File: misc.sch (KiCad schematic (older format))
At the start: 12 parts, among them J11 USB_OTG, U3 RT9193-28, U4 XC6206P302MR

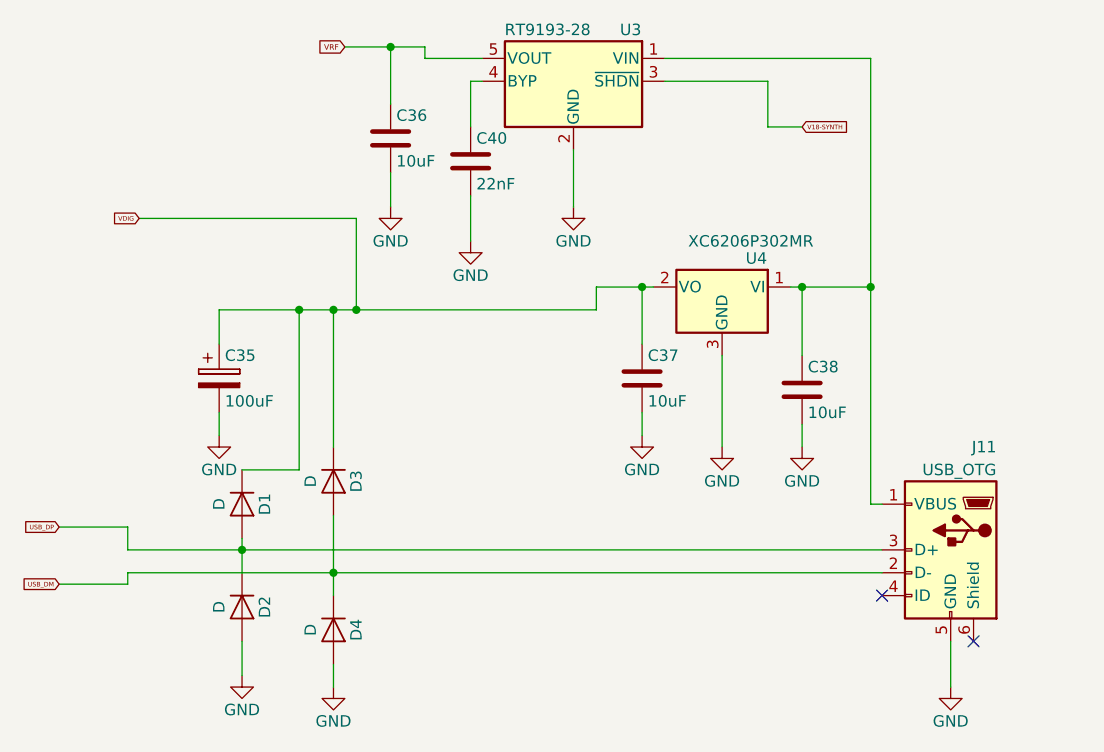
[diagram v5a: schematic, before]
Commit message: use bav99 replace diode
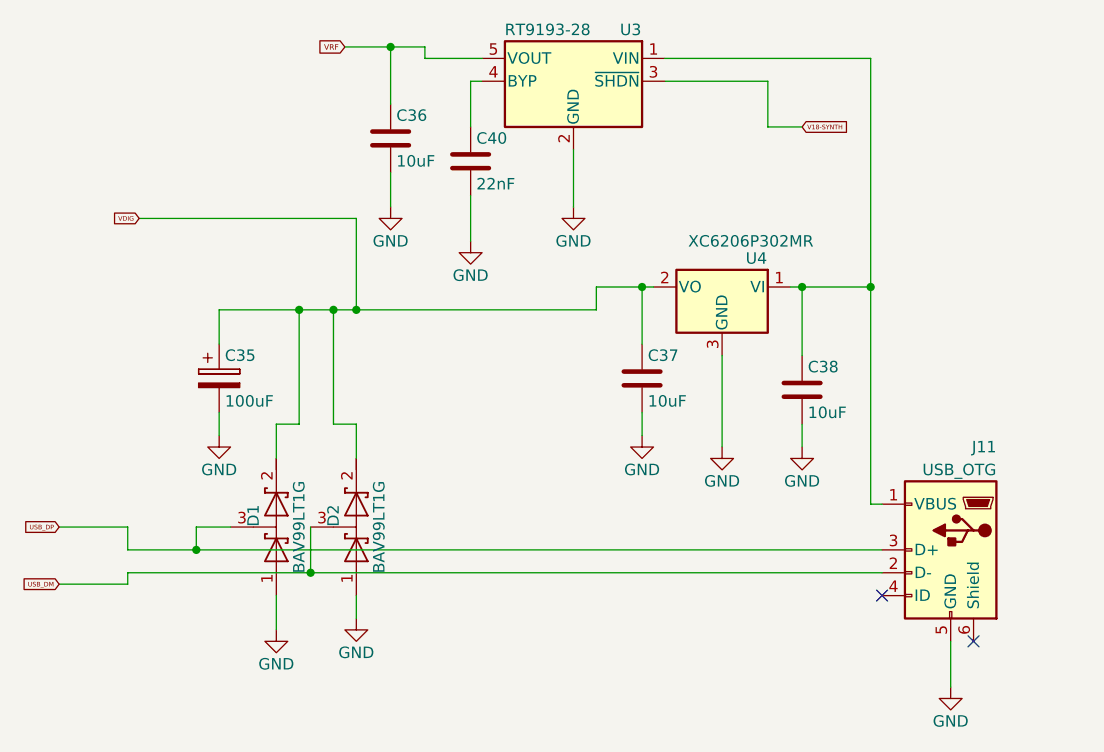
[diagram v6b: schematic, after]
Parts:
- removed D1, D2, D3, D4: D, Diodes_SMD:D_0805, symbol D
- added D1, D2: BAV99LT1G, TO_SOT_Packages_SMD:SOT-23, symbol D_Schottky_x2_Serial_AKC
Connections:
- net GND: now also D1.1 (A), D2.1 (A)
- net USB_DM: now also D2.3 (common)
- net USB_DP: now also D1.3 (common)
- net VDIG: now also D1.2 (K), D2.2 (K)
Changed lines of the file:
@@
 $EndDescr
 $Comp
-L D D1
-U 1 1 5C690C27
-P 4700 3500
-F 0 "D1" H 4700 3600 50  0000 C CNN
-F 1 "D" H 4700 3400 50  0000 C CNN
-F 2 "Diodes_SMD:D_0805" H 4700 3500 50  0001 C CNN
-F 3 "" H 4700 3500 50  0001 C CNN
-	1    4700 3500
-	0    1    1    0
-$EndComp
-$Comp
-L D D2
-U 1 1 5C690CDD
-P 4700 3950
-F 0 "D2" H 4700 4050 50  0000 C CNN
-F 1 "D" H 4700 3850 50  0000 C CNN
-F 2 "Diodes_SMD:D_0805" H 4700 3950 50  0001 C CNN
-F 3 "" H 4700 3950 50  0001 C CNN
-	1    4700 3950
-	0    1    1    0
-$EndComp
-$Comp
-L D D4
-U 1 1 5C690D30
-P 5100 4050
-F 0 "D4" H 5100 4150 50  0000 C CNN
-F 1 "D" H 5100 3950 50  0000 C CNN
-F 2 "Diodes_SMD:D_0805" H 5100 4050 50  0001 C CNN
-F 3 "" H 5100 4050 50  0001 C CNN
-	1    5100 4050
-	0    1    1    0
-$EndComp
-$Comp
-L D D3
-U 1 1 5C690DBF
-P 5100 3400
-F 0 "D3" H 5100 3500 50  0000 C CNN
-F 1 "D" H 5100 3300 50  0000 C CNN
-F 2 "Diodes_SMD:D_0805" H 5100 3400 50  0001 C CNN
-F 3 "" H 5100 3400 50  0001 C CNN
-	1    5100 3400
-	0    1    1    0
-$EndComp
-Wire Wire Line
-	4600 2650 6250 2650
-Wire Wire Line
-	5100 3250 5100 2650
-Connection ~ 5100 2650
-Wire Wire Line
-	5100 3550 5100 3900
-Wire Wire Line
-	4700 3650 4700 3800
-Wire Wire Line
-	4200 3700 7500 3700
-Connection ~ 4700 3700
-Wire Wire Line
-	4200 3800 7500 3800
-Connection ~ 5100 3800
-$Comp
-L GND #PWR037
+L GND #PWR38
 U 1 1 5C690F71
-P 4700 4250
-F 0 "#PWR037" H 4700 4000 50  0001 C CNN
-F 1 "GND" H 4700 4100 50  0000 C CNN
-F 2 "" H 4700 4250 50  0001 C CNN
-F 3 "" H 4700 4250 50  0001 C CNN
-	1    4700 4250
-	1    0    0    -1
-$EndComp
-$Comp
-L GND #PWR038
+P 4850 4050
+F 0 "#PWR38" H 4850 3800 50  0001 C CNN
+F 1 "GND" H 4850 3900 50  0000 C CNN
+F 2 "" H 4850 4050 50  0001 C CNN
+F 3 "" H 4850 4050 50  0001 C CNN
+	1    4850 4050
+	1    0    0    -1
+$EndComp
+$Comp
+L GND #PWR39
 U 1 1 5C690F9B
-P 5100 4300
-F 0 "#PWR038" H 5100 4050 50  0001 C CNN
-F 1 "GND" H 5100 4150 50  0000 C CNN
-F 2 "" H 5100 4300 50  0001 C CNN
-F 3 "" H 5100 4300 50  0001 C CNN
-	1    5100 4300
-	1    0    0    -1
-$EndComp
-Wire Wire Line
-	5100 4300 5100 4200
-Wire Wire Line
-	4700 4250 4700 4100
-Wire Wire Line
-	4700 3350 4950 3350
-Wire Wire Line
-	4950 3350 4950 2650
+P 5200 4000
+F 0 "#PWR39" H 5200 3750 50  0001 C CNN
+F 1 "GND" H 5200 3850 50  0000 C CNN
+F 2 "" H 5200 4000 50  0001 C CNN
+F 3 "" H 5200 4000 50  0001 C CNN
+	1    5200 4000
+	1    0    0    -1
+$EndComp
 Text GLabel 4250 2250 0    20   Input ~ 0
 VDIG
-Wire Wire Line
-	4250 2250 5200 2250
-Wire Wire Line
-	5200 2250 5200 2650
-Connection ~ 5200 2650
 Text GLabel 3900 3850 0    20   Input ~ 0
 USB_DM
 Text GLabel 3900 3600 0    20   Input ~ 0
 USB_DP
-Wire Wire Line
-	4200 3700 4200 3600
-Wire Wire Line
-	4200 3600 3900 3600
-Wire Wire Line
-	4200 3800 4200 3850
-Wire Wire Line
-	4200 3850 3900 3850
-$Comp
-L GND #PWR039
+$Comp
+L GND #PWR37
 U 1 1 5C6911FA
 P 4600 3200
-F 0 "#PWR039" H 4600 2950 50  0001 C CNN
+F 0 "#PWR37" H 4600 2950 50  0001 C CNN
 F 1 "GND" H 4600 3050 50  0000 C CNN
 F 2 "" H 4600 3200 50  0001 C CNN
@@
 	1    0    0    -1
 $EndComp
-Wire Wire Line
-	6450 2800 6450 2550
-Wire Wire Line
-	6250 2550 6500 2550
-Wire Wire Line
-	7100 2550 7450 2550
-Wire Wire Line
-	7150 2550 7150 2850
-$Comp
-L GND #PWR040
+$Comp
+L GND #PWR44
 U 1 1 5C691B40
 P 6800 3250
-F 0 "#PWR040" H 6800 3000 50  0001 C CNN
+F 0 "#PWR44" H 6800 3000 50  0001 C CNN
 F 1 "GND" H 6800 3100 50  0000 C CNN
 F 2 "" H 6800 3250 50  0001 C CNN
@@
 	1    0    0    -1
 $EndComp
-Wire Wire Line
-	6800 3250 6800 2850
-Wire Wire Line
-	6250 2650 6250 2550
-Connection ~ 6450 2550
-Wire Wire Line
-	7450 1550 7450 3500
-Connection ~ 7150 2550
-$Comp
-L GND #PWR041
+$Comp
+L GND #PWR43
 U 1 1 5C692086
 P 6450 3200
-F 0 "#PWR041" H 6450 2950 50  0001 C CNN
+F 0 "#PWR43" H 6450 2950 50  0001 C CNN
 F 1 "GND" H 6450 3050 50  0000 C CNN
 F 2 "" H 6450 3200 50  0001 C CNN
@@
 $EndComp
 $Comp
-L GND #PWR042
+L GND #PWR45
 U 1 1 5C6920B8
 P 7150 3250
-F 0 "#PWR042" H 7150 3000 50  0001 C CNN
+F 0 "#PWR45" H 7150 3000 50  0001 C CNN
 F 1 "GND" H 7150 3100 50  0000 C CNN
 F 2 "" H 7150 3250 50  0001 C CNN
@@
 	1    0    0    -1
 $EndComp
-Wire Wire Line
-	6450 3200 6450 3100
-Wire Wire Line
-	7150 3250 7150 3150
-$Comp
-L GND #PWR043
+$Comp
+L GND #PWR42
 U 1 1 5C69221A
 P 6150 2200
-F 0 "#PWR043" H 6150 1950 50  0001 C CNN
+F 0 "#PWR42" H 6150 1950 50  0001 C CNN
 F 1 "GND" H 6150 2050 50  0000 C CNN
 F 2 "" H 6150 2200 50  0001 C CNN
@@
 Text GLabel 5150 1500 0    24   Input ~ 0
 VRF
-Wire Wire Line
-	5500 1550 5750 1550
-Wire Wire Line
-	5500 1550 5500 1500
-Wire Wire Line
-	5500 1500 5150 1500
 Text GLabel 7150 1850 2    20   Input ~ 0
 V18-SYNTH
-Wire Wire Line
-	7150 1850 7000 1850
-Wire Wire Line
-	7000 1850 7000 1650
-Wire Wire Line
-	7000 1650 6550 1650
 $Comp
 L C C36
@@
 	1    0    0    -1
 $EndComp
-Wire Wire Line
-	5350 1750 5350 1500
-Connection ~ 5350 1500
-$Comp
-L GND #PWR044
+$Comp
+L GND #PWR40
 U 1 1 5C692712
 P 5350 2200
-F 0 "#PWR044" H 5350 1950 50  0001 C CNN
+F 0 "#PWR40" H 5350 1950 50  0001 C CNN
 F 1 "GND" H 5350 2050 50  0000 C CNN
 F 2 "" H 5350 2200 50  0001 C CNN
@@
 	1    0    0    -1
 $EndComp
-Wire Wire Line
-	5350 2200 5350 2050
-Wire Wire Line
-	6550 1550 7450 1550
-Connection ~ 7450 2550
-Wire Wire Line
-	6150 1950 6150 2200
-$Comp
-L GND #PWR045
+$Comp
+L GND #PWR46
 U 1 1 5C693D92
 P 7800 4300
-F 0 "#PWR045" H 7800 4050 50  0001 C CNN
+F 0 "#PWR46" H 7800 4050 50  0001 C CNN
 F 1 "GND" H 7800 4150 50  0000 C CNN
 F 2 "" H 7800 4300 50  0001 C CNN
@@
 	1    0    0    -1
 $EndComp
-Wire Wire Line
-	7800 4300 7800 4100
 $Comp
 L USB_OTG J11
@@
 NoConn ~ 7500 3900
 NoConn ~ 7900 4100
-Wire Wire Line
-	7450 3500 7500 3500
-Wire Wire Line
-	4600 2650 4600 2800
-Connection ~ 4950 2650
 $Comp
 L CP C35
@@
 	1    0    0    -1
 $EndComp
-Wire Wire Line
-	4600 3200 4600 3100
 $Comp
 L APE8865NR-30-HF-3 U4
@@
 $EndComp
 $Comp
-L GND #PWR046
+L GND #PWR41
 U 1 1 5CB1E8F3
 P 5700 2350
-F 0 "#PWR046" H 5700 2100 50  0001 C CNN
+F 0 "#PWR41" H 5700 2100 50  0001 C CNN
 F 1 "GND" H 5700 2200 50  0000 C CNN
 F 2 "" H 5700 2350 50  0001 C CNN
@@
 	1    0    0    -1
 $EndComp
+$Comp
+L D_Schottky_x2_Serial_AKC D1
+U 1 1 5CBC63C6
+P 4850 3600
+F 0 "D1" H 4900 3500 50  0000 C CNN
+F 1 "BAV99LT1G" H 4850 3700 50  0000 C CNN
+F 2 "TO_SOT_Packages_SMD:SOT-23" H 4850 3600 50  0001 C CNN
+F 3 "" H 4850 3600 50  0001 C CNN
+	1    4850 3600
+	0    1    -1   0
+$EndComp
+$Comp
+L D_Schottky_x2_Serial_AKC D2
+U 1 1 5CBC651E
+P 5200 3600
+F 0 "D2" H 5250 3500 50  0000 C CNN
+F 1 "BAV99LT1G" H 5200 3700 50  0000 C CNN
+F 2 "TO_SOT_Packages_SMD:SOT-23" H 5200 3600 50  0001 C CNN
+F 3 "" H 5200 3600 50  0001 C CNN
+	1    5200 3600
+	0    1    -1   0
+$EndComp
+Wire Wire Line
+	4600 2650 6250 2650
+Connection ~ 5100 2650
+Wire Wire Line
+	4200 3700 7500 3700
+Wire Wire Line
+	4200 3800 7500 3800
+Wire Wire Line
+	5200 4000 5200 3900
+Wire Wire Line
+	4850 4050 4850 3900
+Wire Wire Line
+	4250 2250 5200 2250
+Wire Wire Line
+	5200 2250 5200 2650
+Connection ~ 5200 2650
+Wire Wire Line
+	4200 3700 4200 3600
+Wire Wire Line
+	4200 3600 3900 3600
+Wire Wire Line
+	4200 3800 4200 3850
+Wire Wire Line
+	4200 3850 3900 3850
+Wire Wire Line
+	6450 2800 6450 2550
+Wire Wire Line
+	6250 2550 6500 2550
+Wire Wire Line
+	7100 2550 7450 2550
+Wire Wire Line
+	7150 2550 7150 2850
+Wire Wire Line
+	6800 3250 6800 2850
+Wire Wire Line
+	6250 2650 6250 2550
+Connection ~ 6450 2550
+Wire Wire Line
+	7450 1550 7450 3500
+Connection ~ 7150 2550
+Wire Wire Line
+	6450 3200 6450 3100
+Wire Wire Line
+	7150 3250 7150 3150
+Wire Wire Line
+	5500 1550 5750 1550
+Wire Wire Line
+	5500 1550 5500 1500
+Wire Wire Line
+	5500 1500 5150 1500
+Wire Wire Line
+	7150 1850 7000 1850
+Wire Wire Line
+	7000 1850 7000 1650
+Wire Wire Line
+	7000 1650 6550 1650
+Wire Wire Line
+	5350 1750 5350 1500
+Connection ~ 5350 1500
+Wire Wire Line
+	5350 2200 5350 2050
+Wire Wire Line
+	6550 1550 7450 1550
+Connection ~ 7450 2550
+Wire Wire Line
+	6150 1950 6150 2200
+Wire Wire Line
+	7800 4300 7800 4100
+Wire Wire Line
+	7450 3500 7500 3500
+Wire Wire Line
+	4600 2650 4600 2800
+Connection ~ 4950 2650
+Wire Wire Line
+	4600 3200 4600 3100
 Wire Wire Line
 	5700 1850 5700 1650
@@
 Wire Wire Line
 	5700 2150 5700 2350
+Wire Wire Line
+	4950 2650 4950 3150
+Wire Wire Line
+	4950 3150 4850 3150
+Wire Wire Line
+	4850 3150 4850 3300
+Wire Wire Line
+	5200 3300 5200 3150
+Wire Wire Line
+	5200 3150 5100 3150
+Wire Wire Line
+	5100 3150 5100 2650
+Wire Wire Line
+	4650 3600 4500 3600
+Wire Wire Line
+	4500 3600 4500 3700
+Connection ~ 4500 3700
+Wire Wire Line
+	5000 3600 5000 3800
+Connection ~ 5000 3800
 $EndSCHEMATC

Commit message: pcb version 2
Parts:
- U4: value XC6206P302MR -> AP7313-30SAG
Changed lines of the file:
@@
 P 6800 2550
 F 0 "U4" H 6650 2675 50  0000 C CNN
-F 1 "XC6206P302MR " H 6400 2750 50  0000 L CNN
+F 1 "AP7313-30SAG" H 6400 2750 50  0000 L CNN
 F 2 "TO_SOT_Packages_SMD:SOT-23" H 6800 2775 50  0001 C CIN
 F 3 "" H 6800 2500 50  0001 C CNN
